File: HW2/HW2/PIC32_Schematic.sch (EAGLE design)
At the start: 3 parts

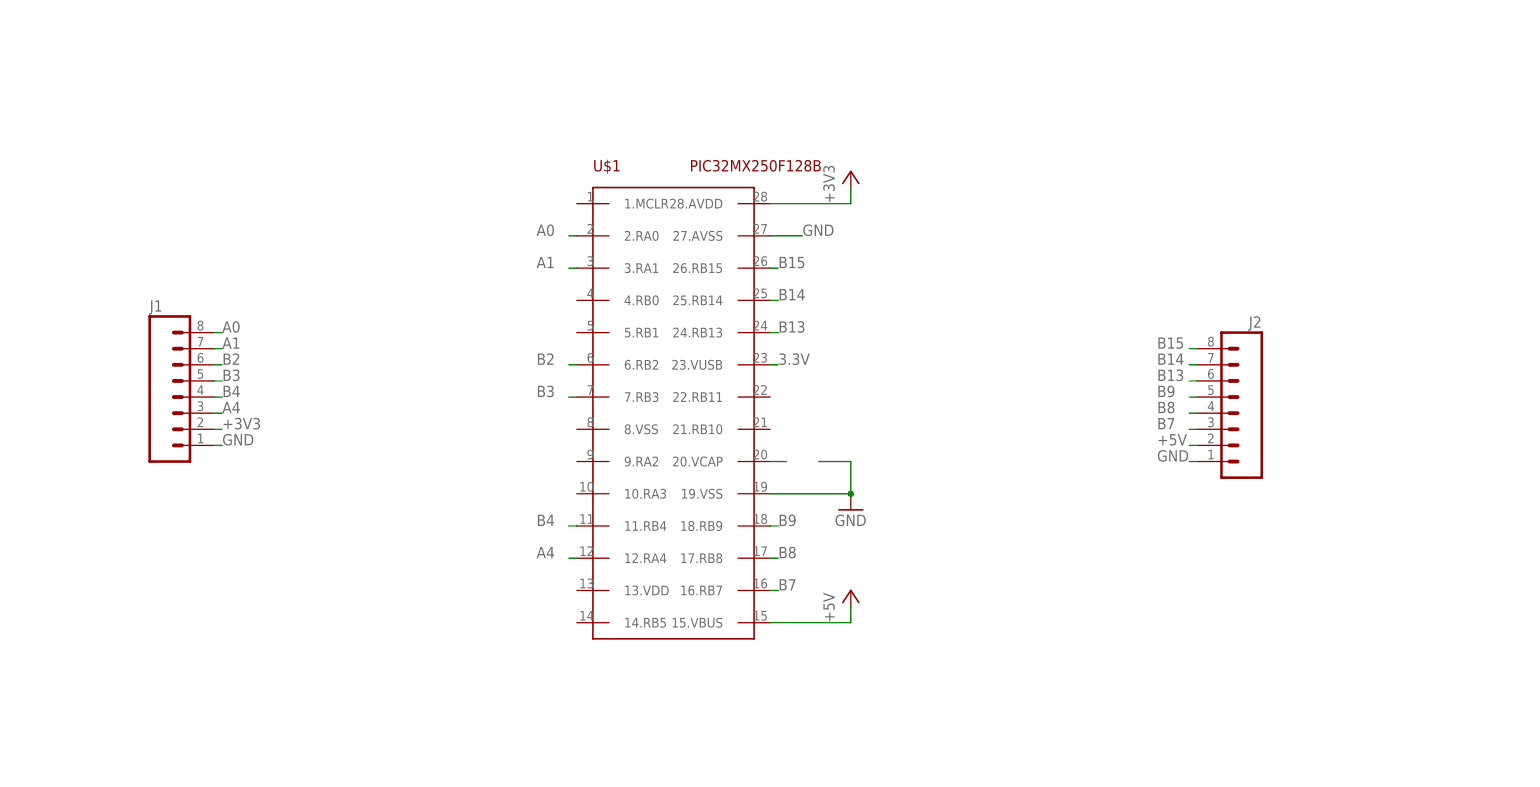
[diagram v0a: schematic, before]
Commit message: Schematic mostly connected (button switches, oscillator, and USB missing)
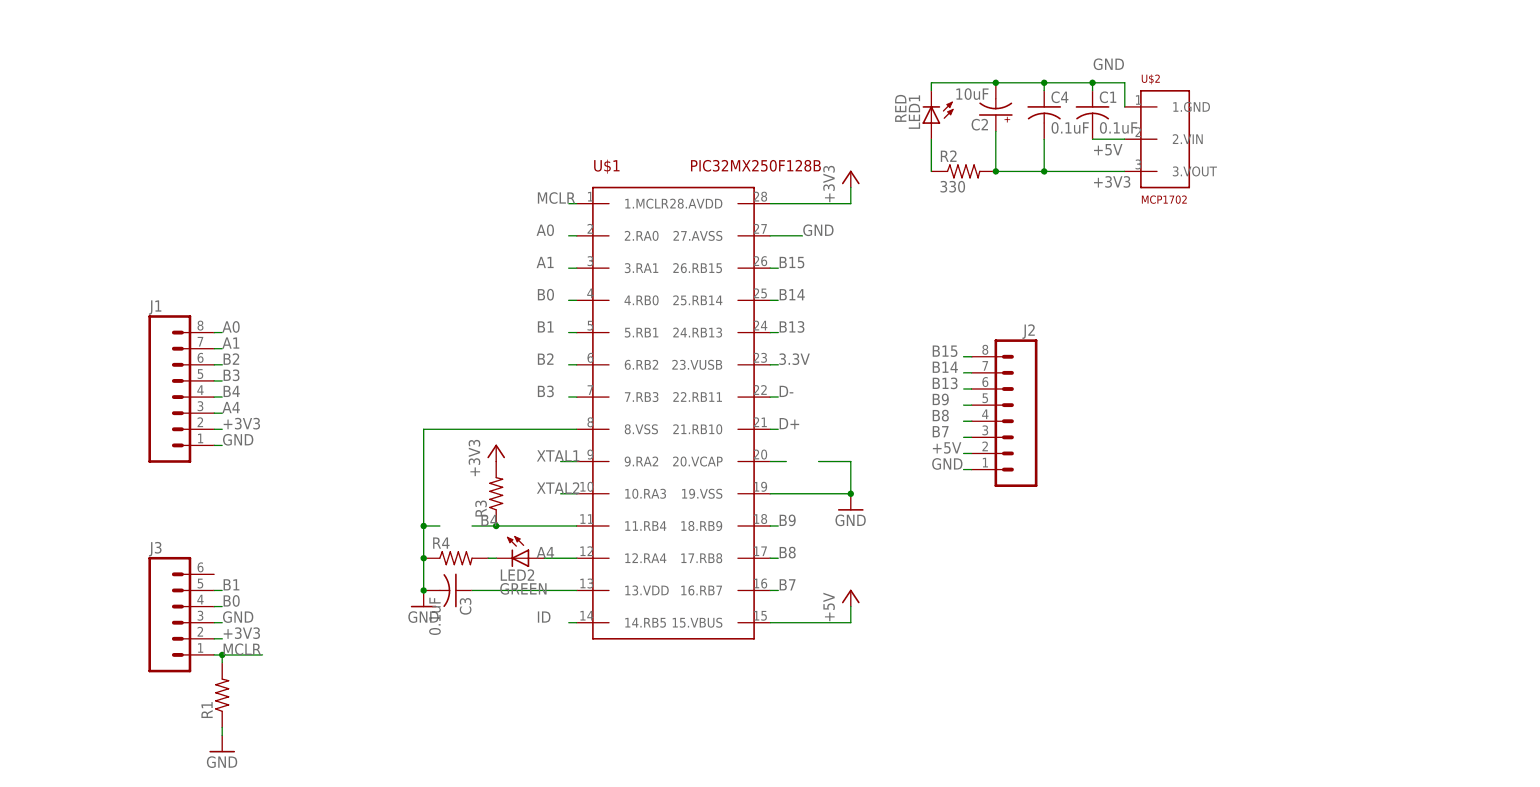
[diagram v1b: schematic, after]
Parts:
- added C1, C3, C4: 0.1uF, ME433:C-US025-024X044
- added C2: 10uF, ME433:CPOL-USTT2D4
- added J3: (no value), ME433:M06SILK_FEMALE_PTH
- added LED1: RED, ME433:LED3MM
- added LED2: GREEN, ME433:LED3MM
- added R1, R3, R4: (no value), ME433:R-US_0207/10
- added R2: 330, ME433:R-US_0207/10
- added U$2: MCP1702, ME433:MCP1702
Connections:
- new net B0: J3.4, U$1.4.RB0
- new net B1: J3.5, U$1.5.RB1
- new net D+: U$1.21.RB10
- new net D-: U$1.22.RB11
- new net ID: U$1.14.RB5
- new net MCLR: J3.1, R1.2, U$1.1.MCLR
- new net N$1: LED1.A, R2.1
- new net N$4: LED2.C, R4.2
- new net N$5: C3.1, U$1.13.VDD
- new net XTAL1: U$1.9.RA2
- new net XTAL2: U$1.10.RA3
- net +3V3: now also C2.+, C4.2, J3.2, R2.2, R3.2, U$2.3.VOUT
- net +5V: now also C1.2, U$2.2.VIN
- net A4: now also LED2.A
- net B4: now also R3.1
- net GND: now also C1.1, C2.-, C3.2, C4.1, J3.3, LED1.C, R1.1, R4.1, U$1.8.VSS, U$2.1.GND
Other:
- moved on the sheet: J2

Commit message: Library is finished and new schematic was started
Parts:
- removed C1, C3, C4: 0.1uF, ME433:C-US025-024X044
- removed C2: 10uF, ME433:CPOL-USTT2D4
- removed J1, J2: (no value), ME433:M08
- removed J3: (no value), ME433:M06SILK_FEMALE_PTH
- removed LED1: RED, ME433:LED3MM
- removed LED2: GREEN, ME433:LED3MM
- removed R1, R3, R4: (no value), ME433:R-US_0207/10
- removed R2: 330, ME433:R-US_0207/10
- removed U$1: PIC32MX250F128B, ME433:PIC32MX250F128B
- removed U$2: MCP1702, ME433:MCP1702
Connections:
- removed net +3V3: C2.+, C4.2, J1.2, J3.2, R2.2, R3.2, U$1.28.AVDD, U$2.3.VOUT
- removed net +5V: C1.2, J2.2, U$1.15.VBUS, U$2.2.VIN
- removed net 3.3V: U$1.23.VUSB
- removed net A0: J1.8, U$1.2.RA0
- removed net A1: J1.7, U$1.3.RA1
- removed net A4: J1.3, LED2.A, U$1.12.RA4
- removed net B0: J3.4, U$1.4.RB0
- removed net B1: J3.5, U$1.5.RB1
- removed net B13: J2.6, U$1.24.RB13
- removed net B14: J2.7, U$1.25.RB14
- removed net B15: J2.8, U$1.26.RB15
- removed net B2: J1.6, U$1.6.RB2
- removed net B3: J1.5, U$1.7.RB3
- removed net B4: J1.4, R3.1, U$1.11.RB4
- removed net B7: J2.3, U$1.16.RB7
- removed net B8: J2.4, U$1.17.RB8
- removed net B9: J2.5, U$1.18.RB9
- removed net D+: U$1.21.RB10
- removed net D-: U$1.22.RB11
- removed net GND: C1.1, C2.-, C3.2, C4.1, J1.1, J2.1, J3.3, LED1.C, R1.1, R4.1, U$1.19.VSS, U$1.27.AVSS, U$1.8.VSS, U$2.1.GND
- removed net ID: U$1.14.RB5
- removed net MCLR: J3.1, R1.2, U$1.1.MCLR
- removed net N$1: LED1.A, R2.1
- removed net N$2: U$1.20.VCAP
- removed net N$4: LED2.C, R4.2
- removed net N$5: C3.1, U$1.13.VDD
- removed net XTAL1: U$1.9.RA2
- removed net XTAL2: U$1.10.RA3

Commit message: New schematic now contains all components
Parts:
- added C1, C2, C3, C4: (no value), ME433:C-US025-024X044
- added C5, C6: (no value), ME433:CPOL-USE2.5-6
- added J1: (no value), ME433:M06SILK_FEMALE_PTH
- added J2, J3: (no value), ME433:M08
- added LED1, LED2: (no value), ME433:LED3MM
- added R1, R2, R3, R4: (no value), ME433:R-US_0207/10
- added U$1: 8MHZ_XTAL, ME433:8MHZ_XTAL
- added U$2: PIC32MX250F128B, ME433:PIC32MX250F128B
- added U$3, U$4: PUSH-BUTTON, ME433:PUSH-BUTTON
- added U$5: SLIDE_SWITCH, ME433:SLIDE_SWITCH
- added U$6: USB-MB-H-5PIN, ME433:USB-MB-H-5PIN
- added U$7: MCP1702, ME433:MCP1702

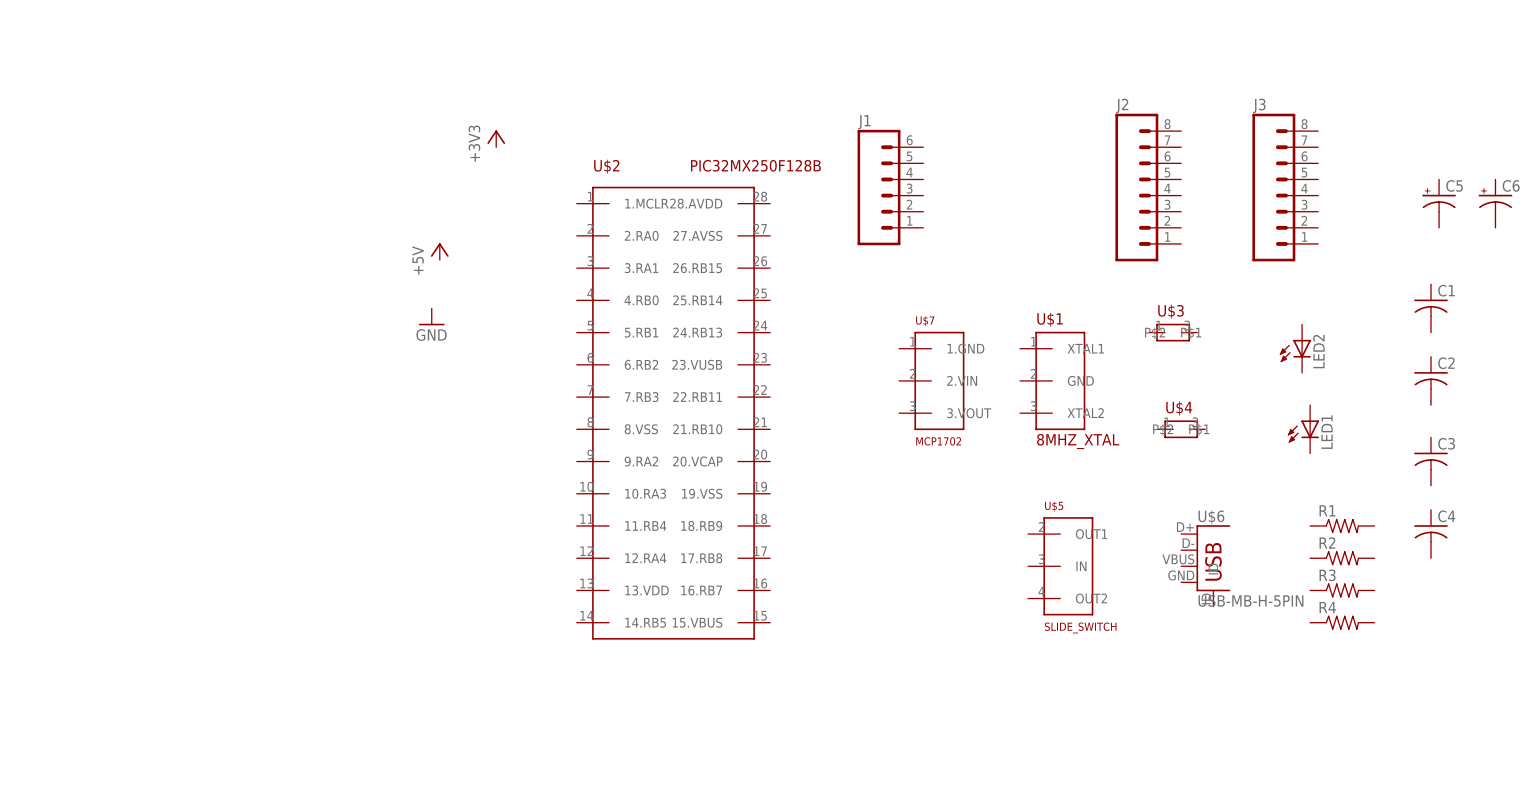
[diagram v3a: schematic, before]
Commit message: XTAL and some pins connected
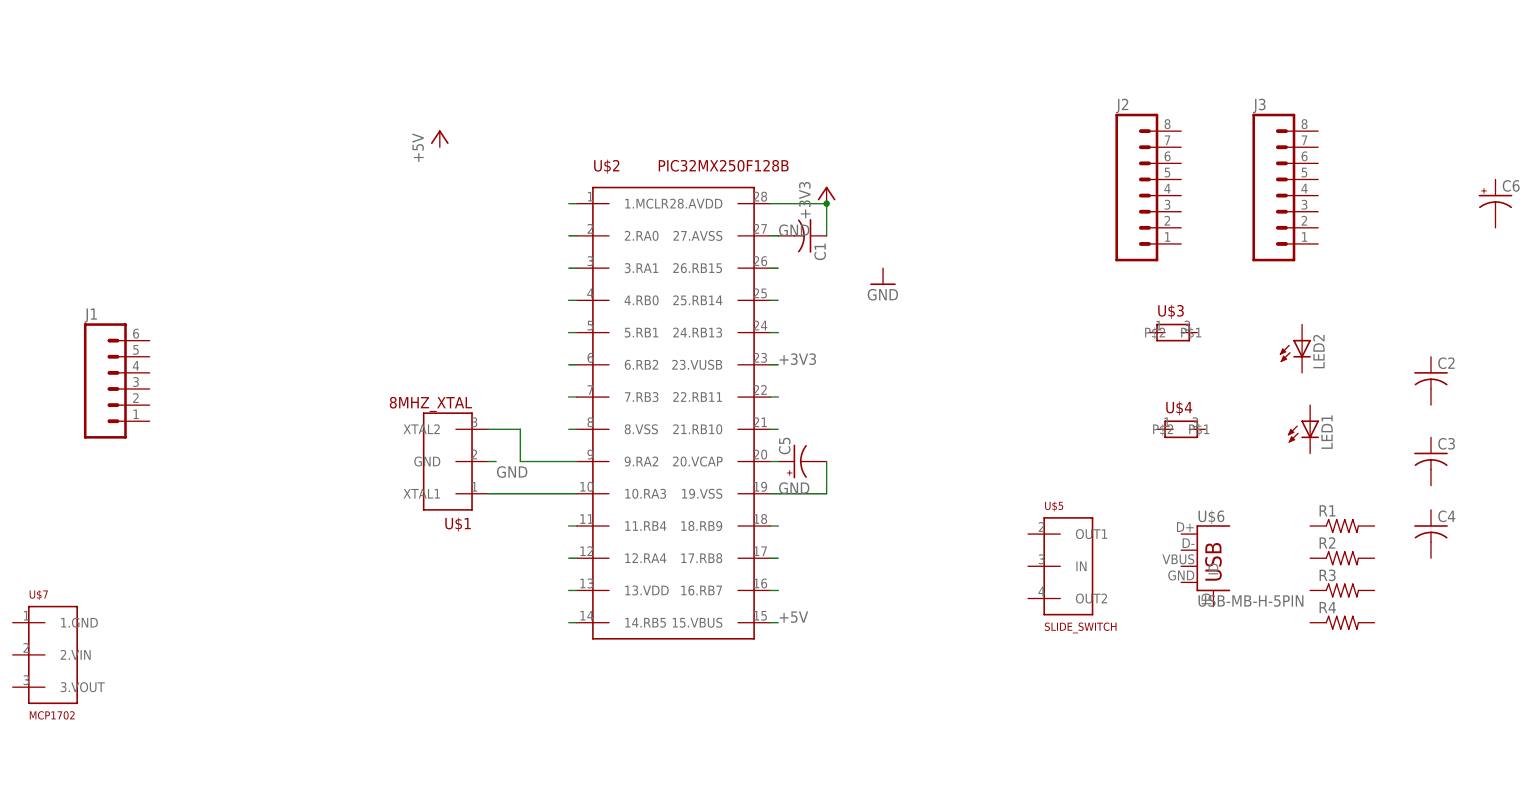
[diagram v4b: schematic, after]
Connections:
- new net +3V3: C1.1, U$2.23.VUSB, U$2.28.AVDD
- new net +5V: U$2.15.VBUS
- new net GND: C1.2, C5.-, U$1.GND, U$1.XTAL2, U$2.19.VSS, U$2.27.AVSS, U$2.9.RA2
- new net N$11: U$2.18.RB9
- new net N$12: U$2.17.RB8
- new net N$13: U$2.16.RB7
- new net N$15: U$2.14.RB5
- new net N$16: U$2.13.VDD
- new net N$17: U$2.12.RA4
- new net N$18: U$2.11.RB4
- new net N$19: U$1.XTAL1, U$2.10.RA3
- new net N$21: U$2.8.VSS
- new net N$22: U$2.7.RB3
- new net N$23: U$2.6.RB2
- new net N$24: U$2.5.RB1
- new net N$25: U$2.4.RB0
- new net N$26: U$2.3.RA1
- new net N$27: U$2.2.RA0
- new net N$28: U$2.1.MCLR
- new net N$3: U$2.26.RB15
- new net N$4: U$2.25.RB14
- new net N$5: U$2.24.RB13
- new net N$7: U$2.22.RB11
- new net N$8: U$2.21.RB10
- new net N$9: C5.+, U$2.20.VCAP
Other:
- moved on the sheet: C1, C5, J1, U$1, U$7
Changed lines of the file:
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@@
 <setting verticaltext="up"/>
 </settings>
-<grid distance="0.1" unitdist="inch" unit="inch" style="lines" multiple="1" display="no" altdistance="0.01" altunitdist="inch" altunit="inch"/>
+<grid distance="0.05" unitdist="inch" unit="inch" style="lines" multiple="1" display="yes" altdistance="0.025" altunitdist="inch" altunit="inch"/>
 <layers>
 <layer number="1" name="Top" color="4" fill="1" visible="no" active="no"/>
@@
 </plain>
 <instances>
-<instance part="U$1" gate="G$1" x="54.61" y="0"/>
+<instance part="U$1" gate="G$1" x="-29.21" y="-2.54" rot="R180"/>
 <instance part="U$2" gate="G$1" x="0" y="0"/>
 <instance part="U$3" gate="G$1" x="78.74" y="12.7"/>
@@
 <instance part="U$5" gate="G$1" x="63.5" y="-24.13"/>
 <instance part="U$6" gate="G$1" x="85.09" y="-22.86"/>
-<instance part="U$7" gate="G$1" x="40.64" y="5.08"/>
-<instance part="J1" gate="G$1" x="34.29" y="34.29"/>
+<instance part="U$7" gate="G$1" x="-99.06" y="-38.1"/>
+<instance part="J1" gate="G$1" x="-87.63" y="3.81"/>
 <instance part="J2" gate="G$1" x="74.93" y="34.29"/>
 <instance part="J3" gate="G$1" x="96.52" y="34.29"/>
@@
 <instance part="R3" gate="G$1" x="105.41" y="-27.94"/>
 <instance part="R4" gate="G$1" x="105.41" y="-33.02"/>
-<instance part="C1" gate="G$1" x="119.38" y="17.78"/>
+<instance part="C1" gate="G$1" x="21.59" y="27.94" rot="R270"/>
 <instance part="C2" gate="G$1" x="119.38" y="6.35"/>
 <instance part="C3" gate="G$1" x="119.38" y="-6.35"/>
 <instance part="C4" gate="G$1" x="119.38" y="-17.78"/>
-<instance part="C5" gate="G$1" x="120.65" y="34.29"/>
+<instance part="C5" gate="G$1" x="19.05" y="-7.62" rot="R90"/>
 <instance part="C6" gate="G$1" x="129.54" y="34.29"/>
-<instance part="+3V1" gate="G$1" x="-27.94" y="44.45"/>
-<instance part="P+1" gate="1" x="-36.83" y="26.67"/>
-<instance part="GND1" gate="1" x="-38.1" y="13.97"/>
+<instance part="+3V1" gate="G$1" x="24.13" y="35.56"/>
+<instance part="P+1" gate="1" x="-36.83" y="44.45"/>
+<instance part="GND1" gate="1" x="33.02" y="20.32"/>
 </instances>
 <busses>
 </busses>
 <nets>
+<net name="N$3" class="0">
+<segment>
+<pinref part="U$2" gate="G$1" pin="26.RB15"/>
+<wire x1="15.24" y1="22.86" x2="16.51" y2="22.86" width="0.1524" layer="91"/>
+</segment>
+</net>
+<net name="N$4" class="0">
+<segment>
+<pinref part="U$2" gate="G$1" pin="25.RB14"/>
+<wire x1="15.24" y1="17.78" x2="16.51" y2="17.78" width="0.1524" layer="91"/>
+</segment>
+</net>
+<net name="N$5" class="0">
+<segment>
+<pinref part="U$2" gate="G$1" pin="24.RB13"/>
+<wire x1="15.24" y1="12.7" x2="16.51" y2="12.7" width="0.1524" layer="91"/>
+</segment>
+</net>
+<net name="N$7" class="0">
+<segment>
+<pinref part="U$2" gate="G$1" pin="22.RB11"/>
+<wire x1="15.24" y1="2.54" x2="16.51" y2="2.54" width="0.1524" layer="91"/>
+</segment>
+</net>
+<net name="N$8" class="0">
+<segment>
+<pinref part="U$2" gate="G$1" pin="21.RB10"/>
+<wire x1="15.24" y1="-2.54" x2="16.51" y2="-2.54" width="0.1524" layer="91"/>
+</segment>
+</net>
+<net name="N$9" class="0">
+<segment>
+<pinref part="U$2" gate="G$1" pin="20.VCAP"/>
+<wire x1="15.24" y1="-7.62" x2="16.51" y2="-7.62" width="0.1524" layer="91"/>
+<pinref part="C5" gate="G$1" pin="+"/>
+</segment>
+</net>
+<net name="N$11" class="0">
+<segment>
+<pinref part="U$2" gate="G$1" pin="18.RB9"/>
+<wire x1="15.24" y1="-17.78" x2="16.51" y2="-17.78" width="0.1524" layer="91"/>
+</segment>
+</net>
+<net name="N$12" class="0">
+<segment>
+<pinref part="U$2" gate="G$1" pin="17.RB8"/>
+<wire x1="15.24" y1="-22.86" x2="16.51" y2="-22.86" width="0.1524" layer="91"/>
+</segment>
+</net>
+<net name="N$13" class="0">
+<segment>
+<pinref part="U$2" gate="G$1" pin="16.RB7"/>
+<wire x1="15.24" y1="-27.94" x2="16.51" y2="-27.94" width="0.1524" layer="91"/>
+</segment>
+</net>
+<net name="+5V" class="0">
+<segment>
+<pinref part="U$2" gate="G$1" pin="15.VBUS"/>
+<wire x1="15.24" y1="-33.02" x2="16.51" y2="-33.02" width="0.1524" layer="91"/>
+<label x="16.51" y="-33.02" size="1.778" layer="95"/>
+</segment>
+</net>
+<net name="N$15" class="0">
+<segment>
+<pinref part="U$2" gate="G$1" pin="14.RB5"/>
+<wire x1="-15.24" y1="-33.02" x2="-16.51" y2="-33.02" width="0.1524" layer="91"/>
+</segment>
+</net>
+<net name="N$16" class="0">
+<segment>
+<pinref part="U$2" gate="G$1" pin="13.VDD"/>
+<wire x1="-15.24" y1="-27.94" x2="-16.51" y2="-27.94" width="0.1524" layer="91"/>
+</segment>
+</net>
+<net name="N$17" class="0">
+<segment>
+<pinref part="U$2" gate="G$1" pin="12.RA4"/>
+<wire x1="-15.24" y1="-22.86" x2="-16.51" y2="-22.86" width="0.1524" layer="91"/>
+</segment>
+</net>
+<net name="N$18" class="0">
+<segment>
+<pinref part="U$2" gate="G$1" pin="11.RB4"/>
+<wire x1="-15.24" y1="-17.78" x2="-16.51" y2="-17.78" width="0.1524" layer="91"/>
+</segment>
+</net>
+<net name="N$19" class="0">
+<segment>
+<pinref part="U$2" gate="G$1" pin="10.RA3"/>
+<pinref part="U$1" gate="G$1" pin="XTAL1"/>
+<wire x1="-29.21" y1="-12.7" x2="-15.24" y2="-12.7" width="0.1524" layer="91"/>
+</segment>
+</net>
+<net name="N$21" class="0">
+<segment>
+<pinref part="U$2" gate="G$1" pin="8.VSS"/>
+<wire x1="-15.24" y1="-2.54" x2="-16.51" y2="-2.54" width="0.1524" layer="91"/>
+</segment>
+</net>
+<net name="N$22" class="0">
+<segment>
+<pinref part="U$2" gate="G$1" pin="7.RB3"/>
+<wire x1="-15.24" y1="2.54" x2="-16.51" y2="2.54" width="0.1524" layer="91"/>
+</segment>
+</net>
+<net name="N$23" class="0">
+<segment>
+<pinref part="U$2" gate="G$1" pin="6.RB2"/>
+<wire x1="-15.24" y1="7.62" x2="-16.51" y2="7.62" width="0.1524" layer="91"/>
+</segment>
+</net>
+<net name="N$24" class="0">
+<segment>
+<pinref part="U$2" gate="G$1" pin="5.RB1"/>
+<wire x1="-15.24" y1="12.7" x2="-16.51" y2="12.7" width="0.1524" layer="91"/>
+</segment>
+</net>
+<net name="N$25" class="0">
+<segment>
+<pinref part="U$2" gate="G$1" pin="4.RB0"/>
+<wire x1="-15.24" y1="17.78" x2="-16.51" y2="17.78" width="0.1524" layer="91"/>
+</segment>
+</net>
+<net name="N$26" class="0">
+<segment>
+<pinref part="U$2" gate="G$1" pin="3.RA1"/>
+<wire x1="-15.24" y1="22.86" x2="-16.51" y2="22.86" width="0.1524" layer="91"/>
+</segment>
+</net>
+<net name="N$27" class="0">
+<segment>
+<pinref part="U$2" gate="G$1" pin="2.RA0"/>
+<wire x1="-15.24" y1="27.94" x2="-16.51" y2="27.94" width="0.1524" layer="91"/>
+</segment>
+</net>
+<net name="N$28" class="0">
+<segment>
+<pinref part="U$2" gate="G$1" pin="1.MCLR"/>
+<wire x1="-15.24" y1="33.02" x2="-16.51" y2="33.02" width="0.1524" layer="91"/>
+</segment>
+</net>
+<net name="+3V3" class="0">
+<segment>
+<pinref part="C1" gate="G$1" pin="1"/>
+<pinref part="+3V1" gate="G$1" pin="+3V3"/>
+<wire x1="24.13" y1="27.94" x2="24.13" y2="33.02" width="0.1524" layer="91"/>
+<pinref part="U$2" gate="G$1" pin="28.AVDD"/>
+<wire x1="15.24" y1="33.02" x2="24.13" y2="33.02" width="0.1524" layer="91"/>
+<junction x="24.13" y="33.02"/>
+</segment>
+<segment>
+<pinref part="U$2" gate="G$1" pin="23.VUSB"/>
+<wire x1="15.24" y1="7.62" x2="16.51" y2="7.62" width="0.1524" layer="91"/>
+<label x="16.51" y="7.62" size="1.778" layer="95"/>
+</segment>
+</net>
+<net name="GND" class="0">
+<segment>
+<pinref part="U$2" gate="G$1" pin="19.VSS"/>
+<label x="16.51" y="-12.7" size="1.778" layer="95"/>
+<wire x1="15.24" y1="-12.7" x2="24.13" y2="-12.7" width="0.1524" layer="91"/>
+<pinref part="C5" gate="G$1" pin="-"/>
+<wire x1="24.13" y1="-12.7" x2="24.13" y2="-7.62" width="0.1524" layer="91"/>
+</segment>
+<segment>
+<pinref part="U$2" gate="G$1" pin="27.AVSS"/>
+<wire x1="15.24" y1="27.94" x2="16.51" y2="27.94" width="0.1524" layer="91"/>
+<label x="16.51" y="27.94" size="1.778" layer="95"/>
+<pinref part="C1" gate="G$1" pin="2"/>
+</segment>
+<segment>
+<pinref part="U$2" gate="G$1" pin="9.RA2"/>
+<pinref part="U$1" gate="G$1" pin="XTAL2"/>
+<wire x1="-29.21" y1="-2.54" x2="-24.13" y2="-2.54" width="0.1524" layer="91"/>
+<wire x1="-24.13" y1="-2.54" x2="-24.13" y2="-7.62" width="0.1524" layer="91"/>
+<wire x1="-24.13" y1="-7.62" x2="-15.24" y2="-7.62" width="0.1524" layer="91"/>
+</segment>
+<segment>
+<pinref part="U$1" gate="G$1" pin="GND"/>
+<wire x1="-29.21" y1="-7.62" x2="-27.94" y2="-7.62" width="0.1524" layer="91"/>
+<label x="-27.94" y="-10.16" size="1.778" layer="95"/>
+</segment>
+</net>
 </nets>
 </sheet>
